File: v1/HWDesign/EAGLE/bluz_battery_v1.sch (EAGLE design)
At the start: 10 parts, among them Q1 NTS2101PT1G

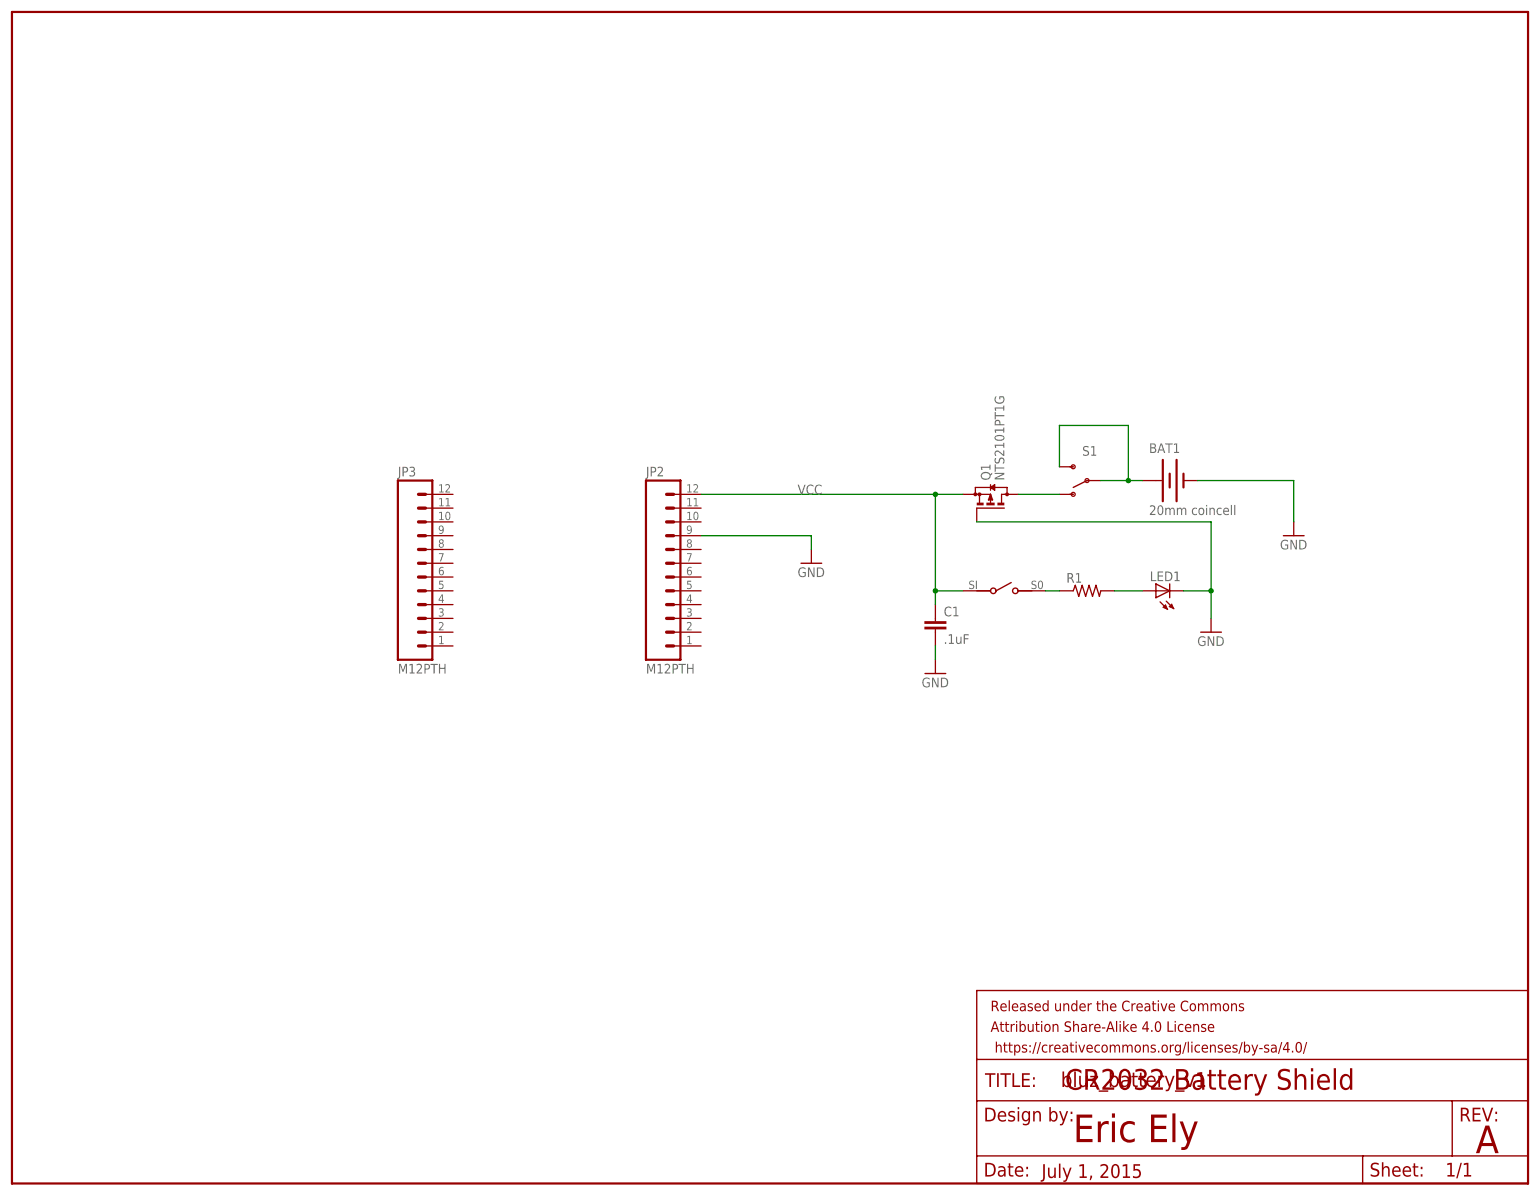
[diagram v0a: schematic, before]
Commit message: changed battery shield to have breakouts and moved switch
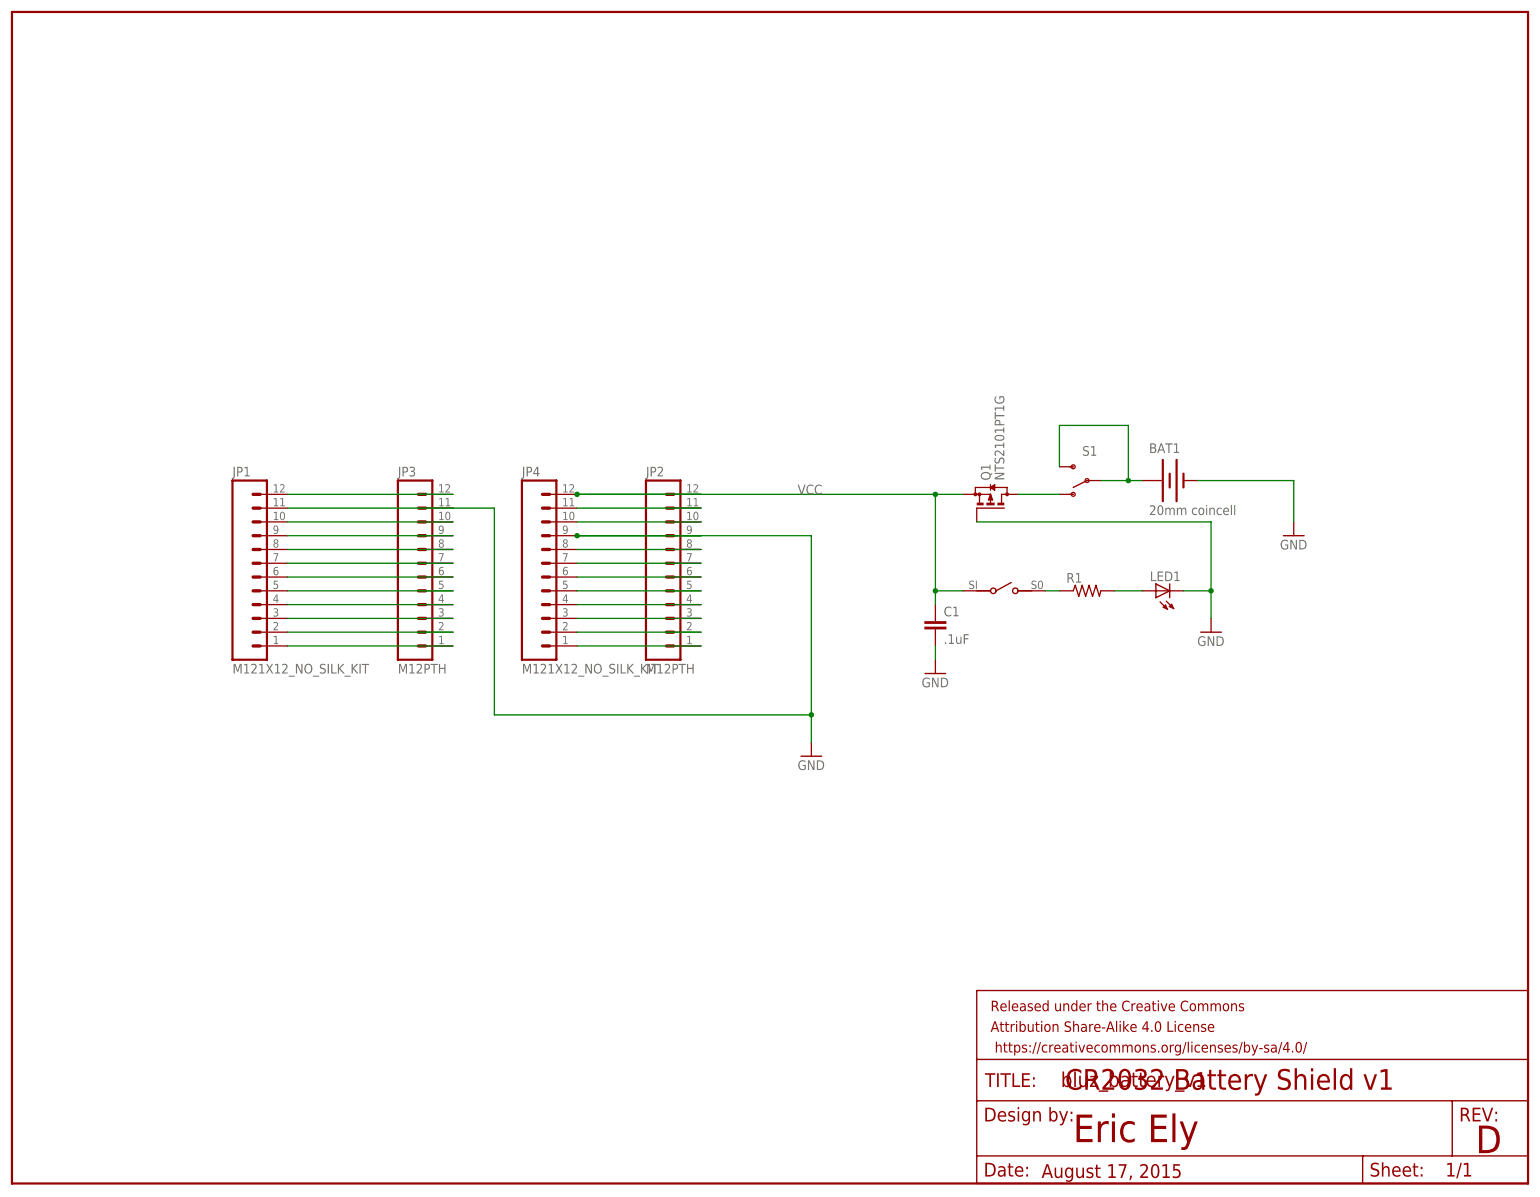
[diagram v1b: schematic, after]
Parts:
- added JP1, JP4: M121X12_NO_SILK_KIT, SparkFun-Connectors:M121X12_NO_SILK_KIT
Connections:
- new net N$10: JP1.6, JP3.6
- new net N$11: JP1.7, JP3.7
- new net N$12: JP1.8, JP3.8
- new net N$13: JP1.9, JP3.9
- new net N$14: JP1.10, JP3.10
- new net N$16: JP1.12, JP3.12
- new net N$17: JP2.1, JP4.1
- new net N$18: JP2.2, JP4.2
- new net N$19: JP2.3, JP4.3
- new net N$2: JP1.1, JP3.1
- new net N$20: JP2.4, JP4.4
- new net N$21: JP2.5, JP4.5
- new net N$22: JP2.6, JP4.6
- new net N$23: JP2.7, JP4.7
- new net N$24: JP2.8, JP4.8
- new net N$25: JP2.10, JP4.10
- new net N$26: JP2.11, JP4.11
- new net N$6: JP1.2, JP3.2
- new net N$7: JP1.3, JP3.3
- new net N$8: JP1.4, JP3.4
- new net N$9: JP1.5, JP3.5
- net GND: now also JP1.11, JP3.11, JP4.9
- net VCC: now also JP4.12
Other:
- note added: "August 17, 2015"
- note added: "CR2032 Battery Shield v1"
- note added: "D"
- note removed: "A"
- note removed: "CR2032 Battery Shield"
- note removed: "July 1, 2015"
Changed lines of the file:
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@@
 <?xml version="1.0" encoding="utf-8"?>
 <!DOCTYPE eagle SYSTEM "eagle.dtd">
-<eagle version="6.5.0">
+<eagle version="7.3.0">
 <drawing>
 <settings>
@@
 <part name="Q1" library="bluze_libr" deviceset="NTS2101PT1G" device=""/>
 <part name="FRAME1" library="SparkFun-Aesthetics" deviceset="FRAME-LETTER" device=""/>
+<part name="JP1" library="SparkFun-Connectors" deviceset="M12" device="1X12_NO_SILK_KIT"/>
+<part name="JP4" library="SparkFun-Connectors" deviceset="M12" device="1X12_NO_SILK_KIT"/>
 </parts>
 <sheets>
@@
 <plain>
 <text x="195.58" y="7.62" size="5.08" layer="94">Eric Ely</text>
-<text x="269.748" y="5.588" size="5.08" layer="94">A</text>
-<text x="189.738" y="1.016" size="2.54" layer="94">July 1, 2015</text>
-<text x="194.056" y="17.272" size="3.81" layer="94">CR2032 Battery Shield</text>
+<text x="269.748" y="5.588" size="5.08" layer="94">D</text>
+<text x="189.738" y="1.016" size="2.54" layer="94">August 17, 2015</text>
+<text x="194.056" y="17.272" size="3.81" layer="94">CR2032 Battery Shield v1</text>
 </plain>
 <instances>
@@
 <instance part="R1" gate="G$1" x="198.12" y="109.22"/>
 <instance part="S1" gate="1" x="198.12" y="129.54" rot="R180"/>
-<instance part="GND1" gate="1" x="147.32" y="114.3"/>
+<instance part="GND1" gate="1" x="147.32" y="78.74"/>
 <instance part="GND2" gate="1" x="236.22" y="119.38"/>
 <instance part="GND3" gate="1" x="170.18" y="93.98"/>
@@
 <attribute name="SHEET" x="264.16" y="1.27" size="2.54" layer="94" font="vector"/>
 </instance>
+<instance part="JP1" gate="G$1" x="40.64" y="114.3"/>
+<instance part="JP4" gate="G$1" x="93.98" y="114.3"/>
 </instances>
 <busses>
@@
 <segment>
 <pinref part="JP2" gate="G$1" pin="9"/>
-<wire x1="127" y1="119.38" x2="147.32" y2="119.38" width="0.1524" layer="91"/>
-<wire x1="147.32" y1="119.38" x2="147.32" y2="116.84" width="0.1524" layer="91"/>
+<wire x1="104.14" y1="119.38" x2="147.32" y2="119.38" width="0.1524" layer="91"/>
+<wire x1="147.32" y1="119.38" x2="147.32" y2="86.36" width="0.1524" layer="91"/>
 <pinref part="GND1" gate="1" pin="GND"/>
+<pinref part="JP4" gate="G$1" pin="9"/>
+<junction x="104.14" y="119.38"/>
+<wire x1="147.32" y1="86.36" x2="147.32" y2="81.28" width="0.1524" layer="91"/>
+<wire x1="104.14" y1="119.38" x2="127" y2="119.38" width="0.1524" layer="91"/>
+<pinref part="JP3" gate="G$1" pin="11"/>
+<pinref part="JP1" gate="G$1" pin="11"/>
+<wire x1="50.8" y1="124.46" x2="81.28" y2="124.46" width="0.1524" layer="91"/>
+<wire x1="81.28" y1="124.46" x2="88.9" y2="124.46" width="0.1524" layer="91"/>
+<wire x1="88.9" y1="124.46" x2="88.9" y2="86.36" width="0.1524" layer="91"/>
+<wire x1="88.9" y1="86.36" x2="147.32" y2="86.36" width="0.1524" layer="91"/>
+<junction x="147.32" y="86.36"/>
 </segment>
 <segment>
@@
 <pinref part="Q1" gate="G$1" pin="S"/>
 <pinref part="JP2" gate="G$1" pin="12"/>
-<wire x1="127" y1="127" x2="170.18" y2="127" width="0.1524" layer="91"/>
+<wire x1="104.14" y1="127" x2="170.18" y2="127" width="0.1524" layer="91"/>
 <junction x="170.18" y="127"/>
+<pinref part="JP4" gate="G$1" pin="12"/>
+<junction x="104.14" y="127"/>
+<wire x1="104.14" y1="127" x2="127" y2="127" width="0.1524" layer="91"/>
 </segment>
 </net>
@@
 </segment>
 </net>
+<net name="N$2" class="0">
+<segment>
+<pinref part="JP3" gate="G$1" pin="1"/>
+<pinref part="JP1" gate="G$1" pin="1"/>
+<wire x1="50.8" y1="99.06" x2="81.28" y2="99.06" width="0.1524" layer="91"/>
+</segment>
+</net>
+<net name="N$6" class="0">
+<segment>
+<pinref part="JP3" gate="G$1" pin="2"/>
+<pinref part="JP1" gate="G$1" pin="2"/>
+<wire x1="50.8" y1="101.6" x2="81.28" y2="101.6" width="0.1524" layer="91"/>
+</segment>
+</net>
+<net name="N$7" class="0">
+<segment>
+<pinref part="JP3" gate="G$1" pin="3"/>
+<pinref part="JP1" gate="G$1" pin="3"/>
+<wire x1="50.8" y1="104.14" x2="81.28" y2="104.14" width="0.1524" layer="91"/>
+</segment>
+</net>
+<net name="N$8" class="0">
+<segment>
+<pinref part="JP3" gate="G$1" pin="4"/>
+<pinref part="JP1" gate="G$1" pin="4"/>
+<wire x1="50.8" y1="106.68" x2="81.28" y2="106.68" width="0.1524" layer="91"/>
+</segment>
+</net>
+<net name="N$9" class="0">
+<segment>
+<pinref part="JP3" gate="G$1" pin="5"/>
+<pinref part="JP1" gate="G$1" pin="5"/>
+<wire x1="50.8" y1="109.22" x2="81.28" y2="109.22" width="0.1524" layer="91"/>
+</segment>
+</net>
+<net name="N$10" class="0">
+<segment>
+<pinref part="JP3" gate="G$1" pin="6"/>
+<pinref part="JP1" gate="G$1" pin="6"/>
+<wire x1="50.8" y1="111.76" x2="81.28" y2="111.76" width="0.1524" layer="91"/>
+</segment>
+</net>
+<net name="N$11" class="0">
+<segment>
+<pinref part="JP3" gate="G$1" pin="7"/>
+<pinref part="JP1" gate="G$1" pin="7"/>
+<wire x1="50.8" y1="114.3" x2="81.28" y2="114.3" width="0.1524" layer="91"/>
+</segment>
+</net>
+<net name="N$12" class="0">
+<segment>
+<pinref part="JP3" gate="G$1" pin="8"/>
+<pinref part="JP1" gate="G$1" pin="8"/>
+<wire x1="50.8" y1="116.84" x2="81.28" y2="116.84" width="0.1524" layer="91"/>
+</segment>
+</net>
+<net name="N$13" class="0">
+<segment>
+<pinref part="JP3" gate="G$1" pin="9"/>
+<pinref part="JP1" gate="G$1" pin="9"/>
+<wire x1="50.8" y1="119.38" x2="81.28" y2="119.38" width="0.1524" layer="91"/>
+</segment>
+</net>
+<net name="N$14" class="0">
+<segment>
+<pinref part="JP3" gate="G$1" pin="10"/>
+<pinref part="JP1" gate="G$1" pin="10"/>
+<wire x1="50.8" y1="121.92" x2="81.28" y2="121.92" width="0.1524" layer="91"/>
+</segment>
+</net>
+<net name="N$16" class="0">
+<segment>
+<pinref part="JP3" gate="G$1" pin="12"/>
+<pinref part="JP1" gate="G$1" pin="12"/>
+<wire x1="50.8" y1="127" x2="81.28" y2="127" width="0.1524" layer="91"/>
+</segment>
+</net>
+<net name="N$17" class="0">
+<segment>
+<pinref part="JP2" gate="G$1" pin="1"/>
+<pinref part="JP4" gate="G$1" pin="1"/>
+<wire x1="104.14" y1="99.06" x2="127" y2="99.06" width="0.1524" layer="91"/>
+</segment>
+</net>
+<net name="N$18" class="0">
+<segment>
+<pinref part="JP2" gate="G$1" pin="2"/>
+<pinref part="JP4" gate="G$1" pin="2"/>
+<wire x1="104.14" y1="101.6" x2="127" y2="101.6" width="0.1524" layer="91"/>
+</segment>
+</net>
+<net name="N$19" class="0">
+<segment>
+<pinref part="JP2" gate="G$1" pin="3"/>
+<pinref part="JP4" gate="G$1" pin="3"/>
+<wire x1="104.14" y1="104.14" x2="127" y2="104.14" width="0.1524" layer="91"/>
+</segment>
+</net>
+<net name="N$20" class="0">
+<segment>
+<pinref part="JP2" gate="G$1" pin="4"/>
+<pinref part="JP4" gate="G$1" pin="4"/>
+<wire x1="104.14" y1="106.68" x2="127" y2="106.68" width="0.1524" layer="91"/>
+</segment>
+</net>
+<net name="N$21" class="0">
+<segment>
+<pinref part="JP2" gate="G$1" pin="5"/>
+<pinref part="JP4" gate="G$1" pin="5"/>
+<wire x1="104.14" y1="109.22" x2="127" y2="109.22" width="0.1524" layer="91"/>
+</segment>
+</net>
+<net name="N$22" class="0">
+<segment>
+<pinref part="JP2" gate="G$1" pin="6"/>
+<pinref part="JP4" gate="G$1" pin="6"/>
+<wire x1="104.14" y1="111.76" x2="127" y2="111.76" width="0.1524" layer="91"/>
+</segment>
+</net>
+<net name="N$23" class="0">
+<segment>
+<pinref part="JP2" gate="G$1" pin="7"/>
+<pinref part="JP4" gate="G$1" pin="7"/>
+<wire x1="104.14" y1="114.3" x2="127" y2="114.3" width="0.1524" layer="91"/>
+</segment>
+</net>
+<net name="N$24" class="0">
+<segment>
+<pinref part="JP2" gate="G$1" pin="8"/>
+<pinref part="JP4" gate="G$1" pin="8"/>
+<wire x1="104.14" y1="116.84" x2="127" y2="116.84" width="0.1524" layer="91"/>
+</segment>
+</net>
+<net name="N$25" class="0">
+<segment>
+<pinref part="JP2" gate="G$1" pin="10"/>
+<pinref part="JP4" gate="G$1" pin="10"/>
+<wire x1="104.14" y1="121.92" x2="127" y2="121.92" width="0.1524" layer="91"/>
+</segment>
+</net>
+<net name="N$26" class="0">
+<segment>
+<pinref part="JP2" gate="G$1" pin="11"/>
+<pinref part="JP4" gate="G$1" pin="11"/>
+<wire x1="104.14" y1="124.46" x2="127" y2="124.46" width="0.1524" layer="91"/>
+</segment>
+</net>
